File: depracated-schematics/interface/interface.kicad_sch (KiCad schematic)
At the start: 17 parts, among them U1 74LS00, U2 74LS00, U4 74LS245, U5 74LS193, U6 74LS193, U7 74LS193, U8 74LS193

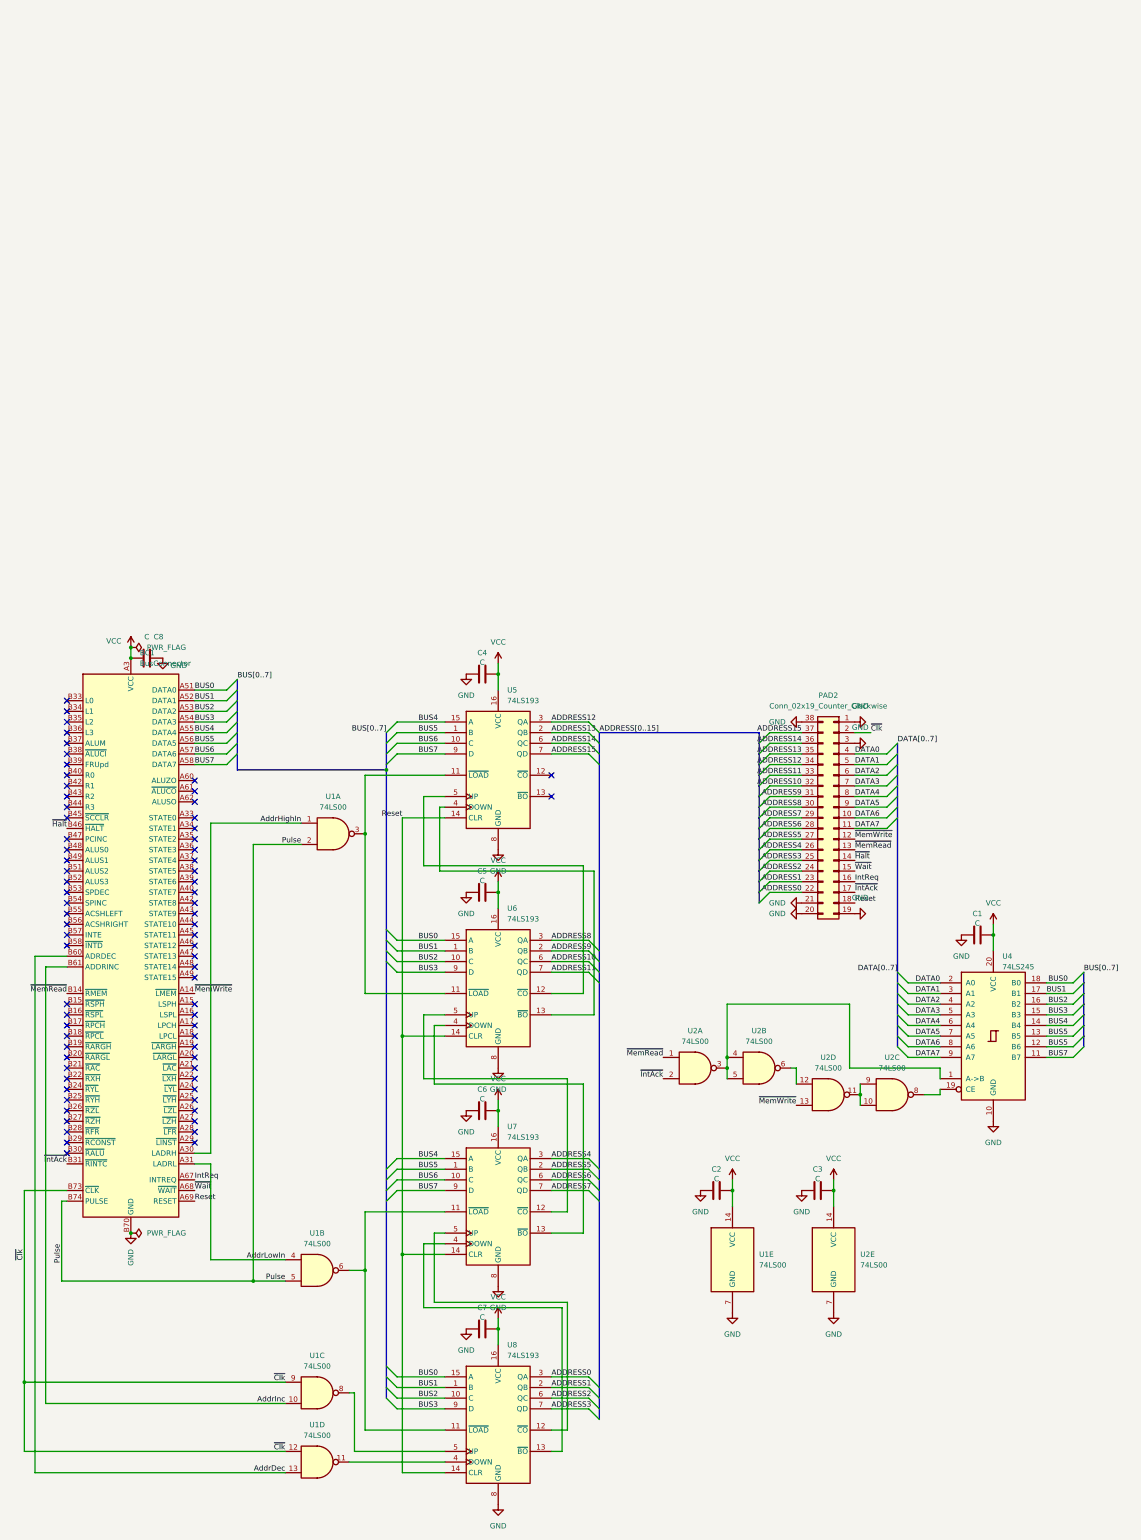
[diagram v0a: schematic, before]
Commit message: structure(kicad): redefined the structure of the repository
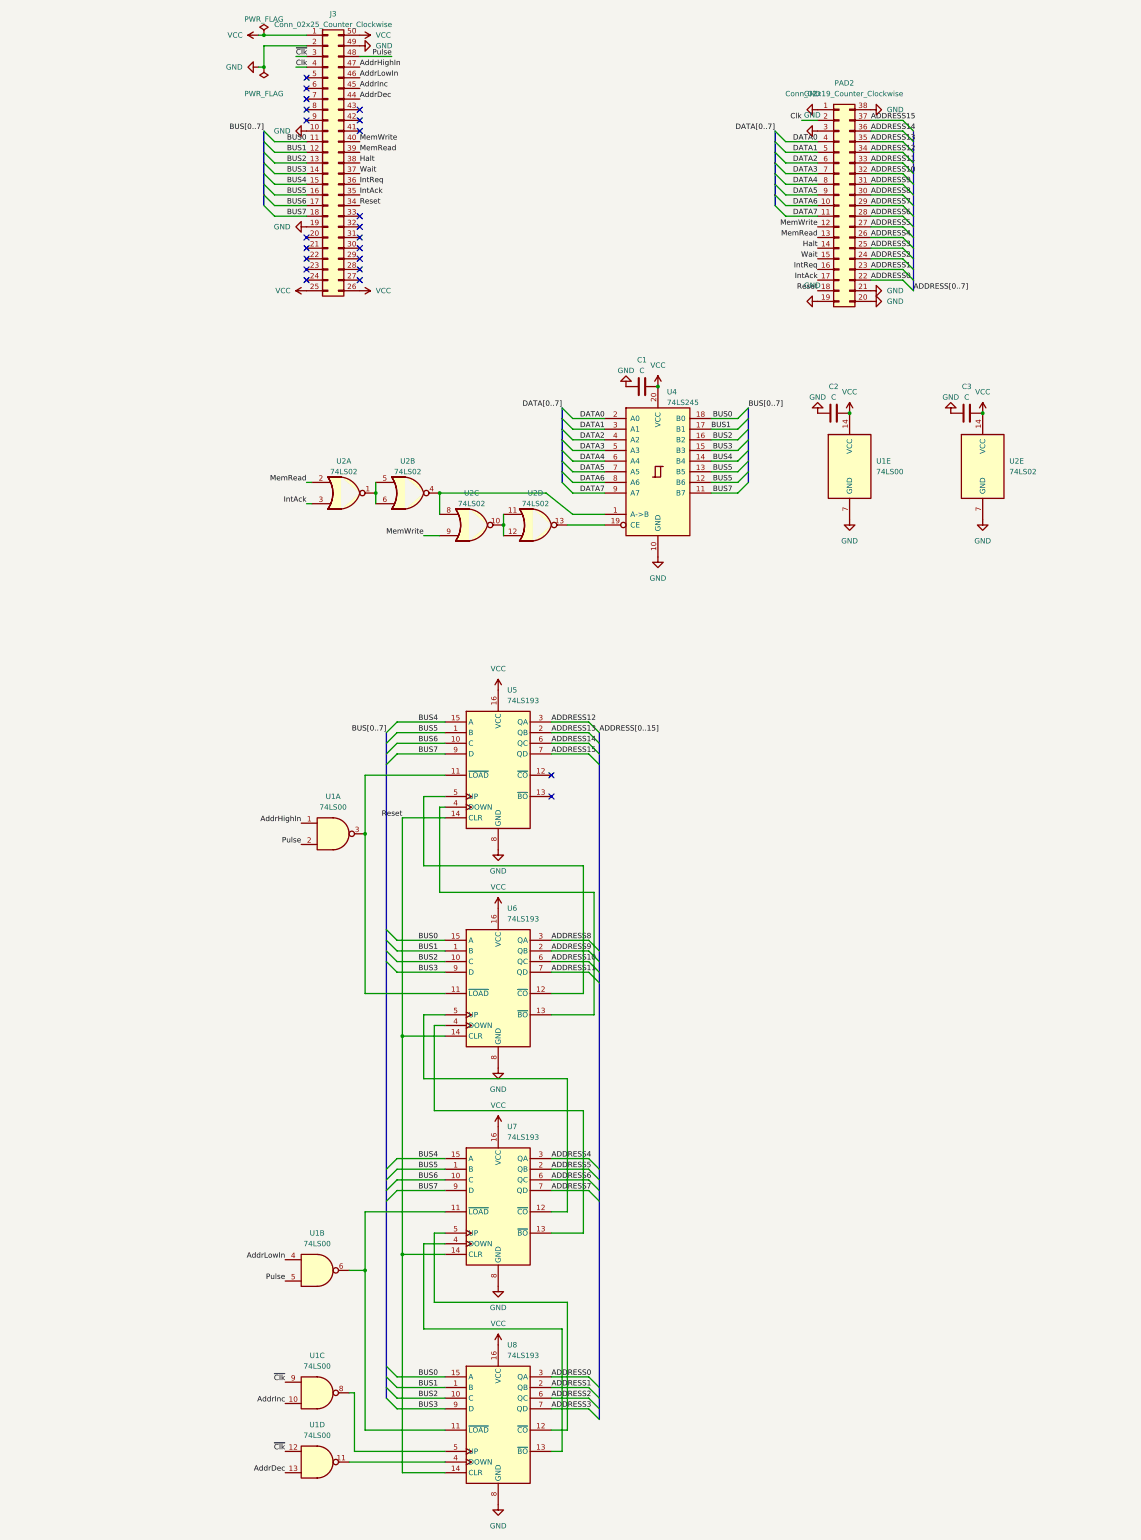
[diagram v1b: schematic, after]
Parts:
- removed BC1: BusConnector, Connector_PCBEdge:BUS_PCIexpress_x16, symbol cpu816symbols:BusConnector
- removed C4, C5, C6, C7: C, Capacitor_THT:C_Disc_D5.0mm_W2.5mm_P5.00mm, symbol Device:C
- removed C8: C, Capacitor_THT:C_Radial_D6.3mm_H5.0mm_P2.50mm, symbol Device:C
- removed U2: 74LS00, Package_DIP:DIP-14_W7.62mm_Socket_LongPads, symbol 74xx:74LS00
- added J3: Conn_02x25_Counter_Clockwise, Connector_PinSocket_2.54mm:PinSocket_2x25_P2.54mm_Horizontal, symbol Connector_Generic:Conn_02x25_Counter_Clockwise
- added U2: 74LS02, Package_DIP:DIP-14_W7.62mm_Socket_LongPads, symbol 74xx:74LS02
- C1, C2, C3: footprint Capacitor_THT:C_Disc_D5.0mm_W2.5mm_P5.00mm -> (none)
- PAD2: footprint Connector_PinSocket_2.54mm:PinSocket_2x19_P2.54mm_Vertical -> Connector_PinSocket_2.54mm:PinSocket_2x19_P2.54mm_Horizontal
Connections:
- net AddrDec: now also J3.44 (Pin_44)
- net AddrHighIn: now also J3.47 (Pin_47)
- net AddrInc: now also J3.45 (Pin_45)
- net AddrLowIn: now also J3.46 (Pin_46)
- net BUS0: now also J3.11 (Pin_11)
- net BUS1: now also J3.12 (Pin_12)
- net BUS2: now also J3.13 (Pin_13)
- net BUS3: now also J3.14 (Pin_14)
- net BUS4: now also J3.15 (Pin_15)
- net BUS5: now also J3.16 (Pin_16)
- net BUS6: now also J3.17 (Pin_17)
- net BUS7: now also J3.18 (Pin_18)
- net GND: now also C1.1, C2.1, C3.1, J3.10 (Pin_10), J3.19 (Pin_19), J3.2 (Pin_2), J3.49 (Pin_49), U2.7 (GND); no longer C1.2, C2.2, C3.2
- net IntReq: now also J3.36 (Pin_36)
- net Pulse: now also J3.48 (Pin_48)
- net Reset: now also J3.34 (Pin_34)
- net VCC: now also C1.2, C2.2, C3.2, J3.1 (Pin_1), J3.25 (Pin_25), J3.26 (Pin_26), J3.50 (Pin_50), U2.14 (VCC); no longer C1.1, C2.1, C3.1
- net ~{Clk}: now also J3.3 (Pin_3); no longer PAD2.2 (Pin_2)
- net at U4.1 (A->B): now also U2.4, U2.8
- net at U4.19 (CE): now also U2.13
- net ~{Halt} renamed Halt
- net Halt: now also J3.38 (Pin_38)
- net ~{IntAck} renamed IntAck
- net IntAck: now also J3.35 (Pin_35), U2.3
- net ~{MemRead} renamed MemRead
- net MemRead: now also J3.39 (Pin_39), U2.2
- net ~{MemWrite} renamed MemWrite
- net MemWrite: now also J3.40 (Pin_40), U2.9
- net ~{Wait} renamed Wait
- net Wait: now also J3.37 (Pin_37)
- new net: U2.1, U2.5, U2.6
- new net: U2.10, U2.11, U2.12
- new net Clk: J3.4 (Pin_4), PAD2.2 (Pin_2)
- no-connect marks 73 -> 22
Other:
- moved on the sheet: PAD2, U1E, U4
